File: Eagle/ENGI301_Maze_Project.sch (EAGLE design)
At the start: 27 parts, among them U3 MOD-LED8X8RGB-CONN, U4 MOD-LED8X8RGB-CONN, U5 CEM-1203, U7 POCKETBEAGLE

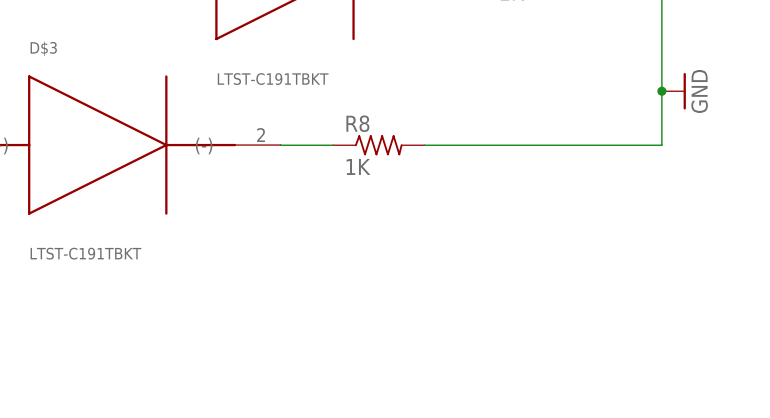
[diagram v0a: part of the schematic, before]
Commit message: Maze Project Eagle Schematic
- Added my name to the title block in the frame
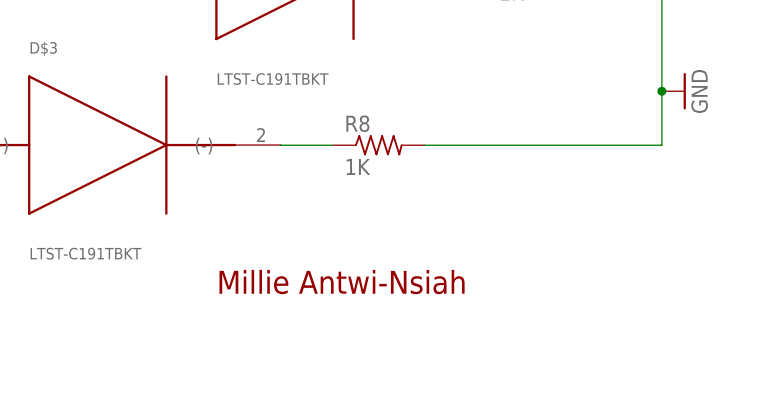
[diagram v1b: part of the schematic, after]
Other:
- note added: "Millie Antwi-Nsiah"
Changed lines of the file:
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@@
 N
 S</text>
+<text x="313.7" y="20.1" size="2.54" layer="94">Millie Antwi-Nsiah</text>
 </plain>
 <instances>
